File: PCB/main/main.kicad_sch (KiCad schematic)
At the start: 70 parts, among them J1 Conn_01x06_Pin, J2 Headlight, J3 Conn_01x05_Pin, J4 Conn_01x03_Pin, J5 Battery, Q1 NPN, Q2 NPN, U1 ESP32-WROOM-32, U2 TB6612FNG, U3 TB6612FNG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

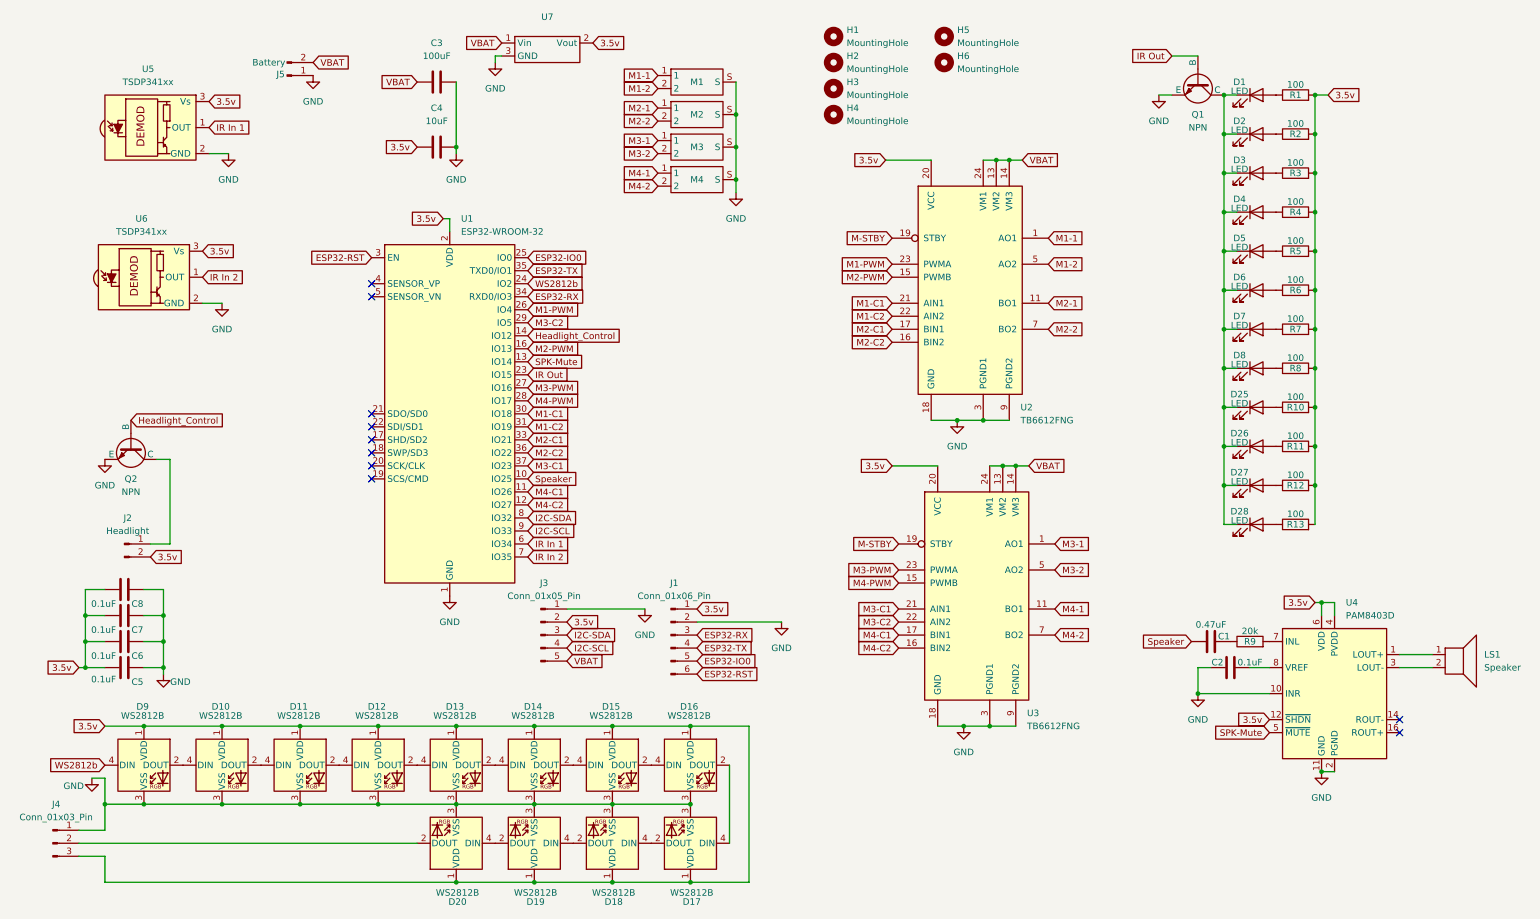
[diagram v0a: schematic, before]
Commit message: Base Resistors and README.md
Added base resistors to the headlight and IR led transistors (facepalm), and added to the main README.md.
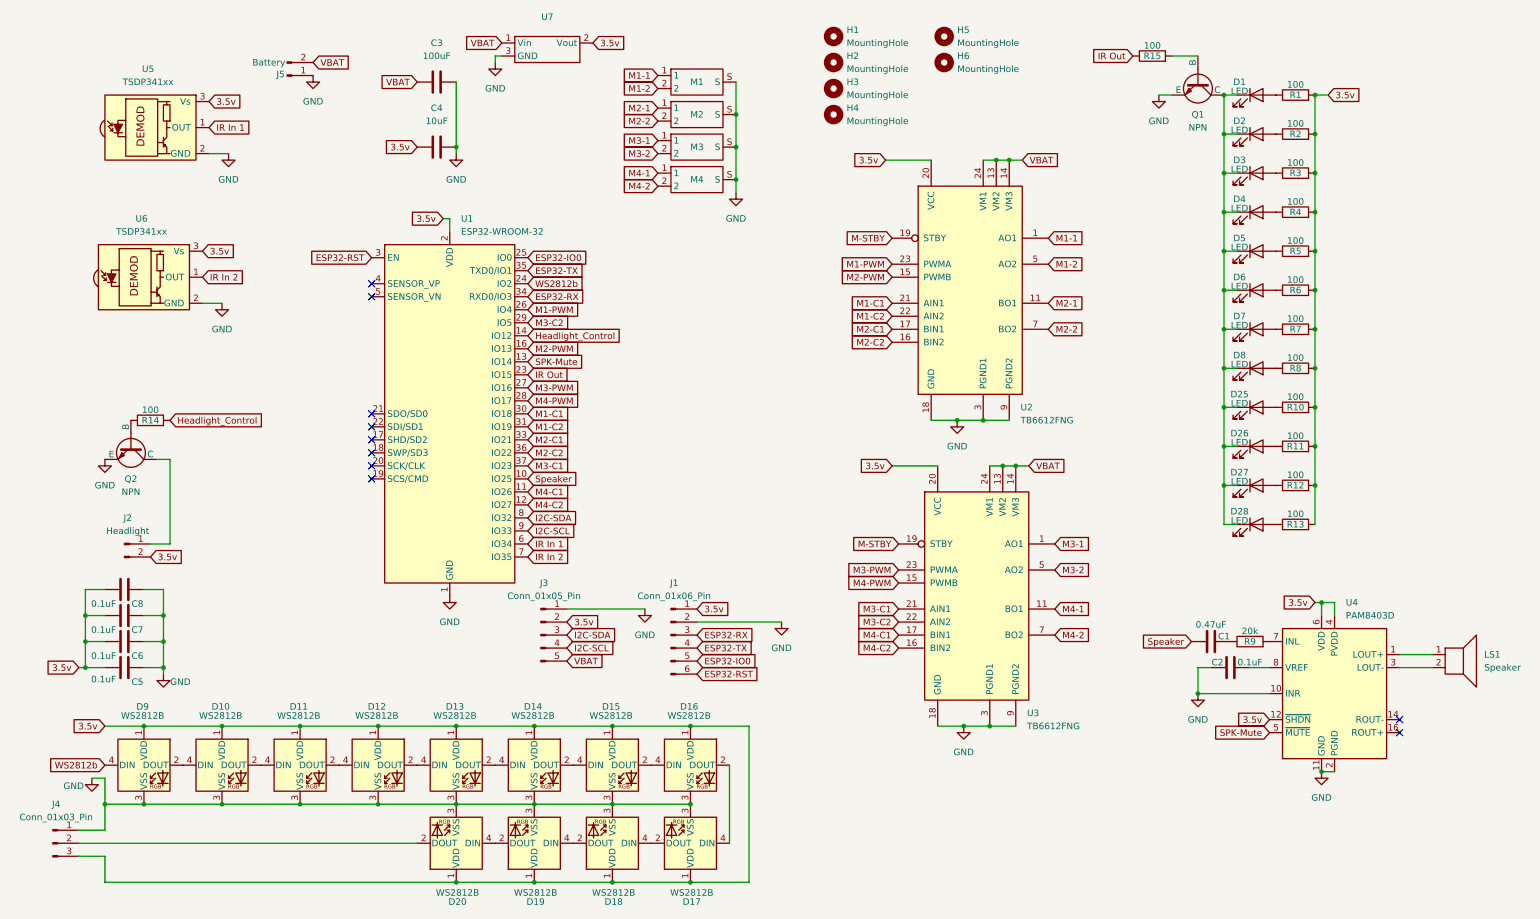
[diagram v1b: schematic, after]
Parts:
- added R14, R15: 100, Resistor_SMD:R_0805_2012Metric_Pad1.20x1.40mm_HandSolder, symbol Device:R
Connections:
- net Headlight_Control: now also R14.2; no longer Q2.2 (B)
- net IR Out: now also R15.1; no longer Q1.2 (B)
- new net: Q1.2 (B), R15.2
- new net: Q2.2 (B), R14.1
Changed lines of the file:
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@@
 	(wire
 		(pts
-			(xy 238.76 21.59) (xy 243.84 21.59)
-		)
-		(stroke
-			(width 0)
-			(type default)
-		)
-	)
-	(wire
-		(pts
 			(xy 251.46 59.69) (xy 248.92 59.69)
 		)
@@
 	(wire
 		(pts
+			(xy 238.76 21.59) (xy 243.84 21.59)
+		)
+		(stroke
+			(width 0)
+			(type default)
+		)
+	)
+	(wire
+		(pts
 			(xy 266.7 74.93) (xy 266.7 82.55)
 		)
@@
 	(global_label "Headlight_Control"
 		(shape input)
-		(at 35.56 92.71 0)
+		(at 43.18 92.71 0)
 		(fields_autoplaced yes)
 		(effects
@@
 		)
 		(property "Intersheetrefs" "${INTERSHEET_REFS}"
-			(at 55.4177 92.71 0)
+			(at 63.0377 92.71 0)
 			(effects
 				(font
@@
 	(global_label "IR Out"
 		(shape input)
-		(at 238.76 21.59 180)
+		(at 231.14 21.59 180)
 		(fields_autoplaced yes)
 		(effects
@@
 		)
 		(property "Intersheetrefs" "${INTERSHEET_REFS}"
-			(at 229.7272 21.59 0)
+			(at 222.1072 21.59 0)
 			(effects
 				(font
@@
 	)
 	(symbol
+		(lib_id "Device:R")
+		(at 234.95 21.59 90)
+		(unit 1)
+		(exclude_from_sim no)
+		(in_bom yes)
+		(on_board yes)
+		(dnp no)
+		(property "Reference" "R15"
+			(at 234.95 21.59 90)
+			(effects
+				(font
+					(size 1.27 1.27)
+				)
+			)
+		)
+		(property "Value" "100"
+			(at 234.95 19.558 90)
+			(effects
+				(font
+					(size 1.27 1.27)
+				)
+			)
+		)
+		(property "Footprint" "Resistor_SMD:R_0805_2012Metric_Pad1.20x1.40mm_HandSolder"
+			(at 234.95 23.368 90)
+			(effects
+				(font
+					(size 1.27 1.27)
+				)
+				(hide yes)
+			)
+		)
+		(property "Datasheet" "~"
+			(at 234.95 21.59 0)
+			(effects
+				(font
+					(size 1.27 1.27)
+				)
+				(hide yes)
+			)
+		)
+		(property "Description" "Resistor"
+			(at 234.95 21.59 0)
+			(effects
+				(font
+					(size 1.27 1.27)
+				)
+				(hide yes)
+			)
+		)
+		(pin "2"
+		)
+		(pin "1"
+		)
+		(instances
+			(project "main"
+				(path "/10a21986-0589-4c3b-a209-3cd4eaf5d331"
+					(reference "R15")
+					(unit 1)
+				)
+			)
+		)
+	)
+	(symbol
 		(lib_id "Device:LED")
 		(at 255.27 97.79 0)
@@
 					(unit 1)
 				)
+			)
+		)
+	)
+	(symbol
+		(lib_id "Device:R")
+		(at 39.37 92.71 90)
+		(unit 1)
+		(exclude_from_sim no)
+		(in_bom yes)
+		(on_board yes)
+		(dnp no)
+		(property "Reference" "R14"
+			(at 39.37 92.71 90)
+			(effects
+				(font
+					(size 1.27 1.27)
+				)
+			)
+		)
+		(property "Value" "100"
+			(at 39.37 90.678 90)
+			(effects
+				(font
+					(size 1.27 1.27)
+				)
+			)
+		)
+		(property "Footprint" "Resistor_SMD:R_0805_2012Metric_Pad1.20x1.40mm_HandSolder"
+			(at 39.37 94.488 90)
+			(effects
+				(font
+					(size 1.27 1.27)
+				)
+				(hide yes)
+			)
+		)
+		(property "Datasheet" "~"
+			(at 39.37 92.71 0)
+			(effects
+				(font
+					(size 1.27 1.27)
+				)
+				(hide yes)
+			)
+		)
+		(property "Description" "Resistor"
+			(at 39.37 92.71 0)
+			(effects
+				(font
+					(size 1.27 1.27)
+				)
+				(hide yes)
+			)
+		)
+		(pin "2"
+		)
+		(pin "1"
+		)
+		(instances
+			(project "main"
+				(path "/10a21986-0589-4c3b-a209-3cd4eaf5d331"
+					(reference "R14")
+					(unit 1)
+				)
